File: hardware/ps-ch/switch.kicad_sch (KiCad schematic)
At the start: 0 parts

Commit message: did some wiring
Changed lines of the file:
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@@
 	(generator_version "9.0")
 	(paper "A4")
-	(hierarchical_label "OFF"
+	(hierarchical_label "ON{slash}~{OFF}"
 		(shape input)
-		(at 74.93 114.3 180)
+		(at 111.76 62.23 0)
 		(effects
 			(font
 				(size 1.27 1.27)
 			)
-			(justify right)
+			(justify left)
 		)
 	)
@@
 		(shape output)
 		(at 171.45 80.01 0)
+		(effects
+			(font
+				(size 1.27 1.27)
+			)
+			(justify left)
+		)
+	)
+	(hierarchical_label "ARM_OUTPUT"
+		(shape input)
+		(at 186.69 113.03 0)
 		(effects
 			(font
@@
 		)
 	)
-	(hierarchical_label "ON"
+	(hierarchical_label "~{OVC}"
 		(shape input)
-		(at 80.01 104.14 180)
+		(at 118.11 118.11 0)
 		(effects
 			(font
 				(size 1.27 1.27)
 			)
-			(justify right)
+			(justify left)
 		)
 	)

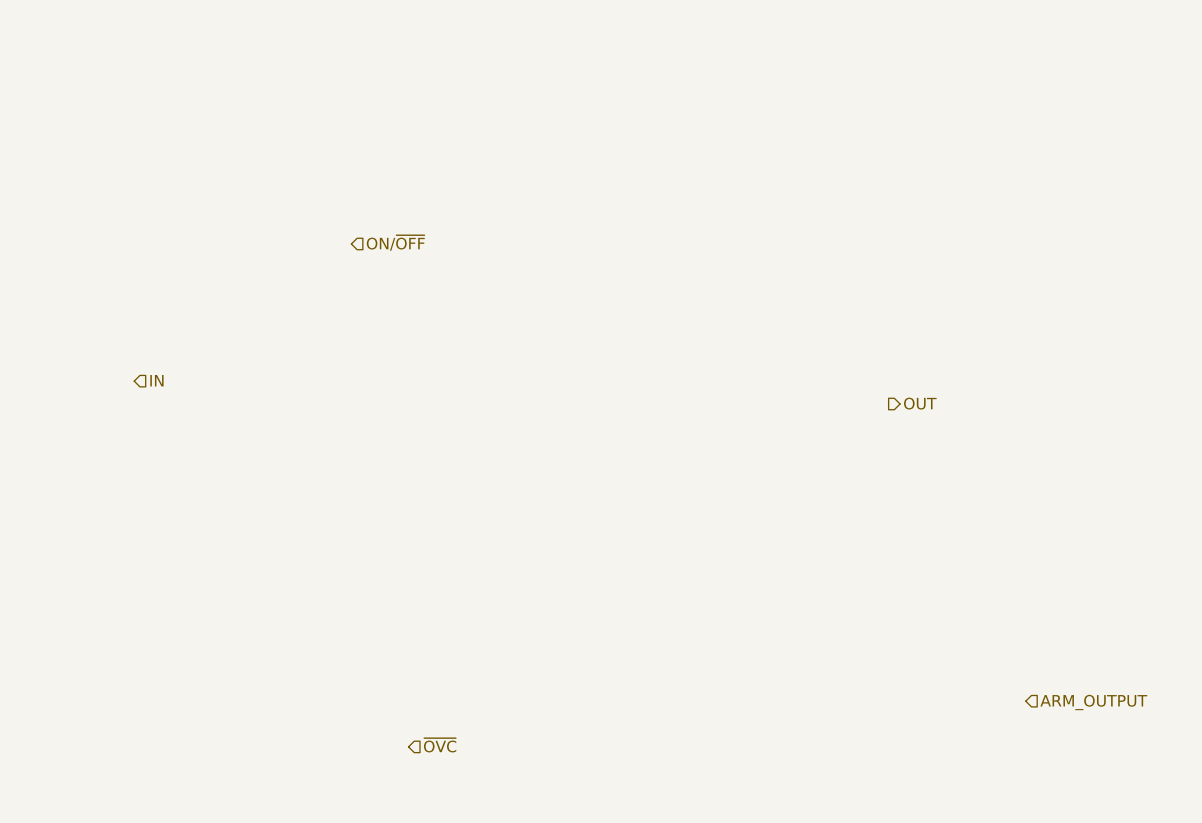
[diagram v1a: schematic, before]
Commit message: more wiring
- updated stm32 pinout
- added load switch
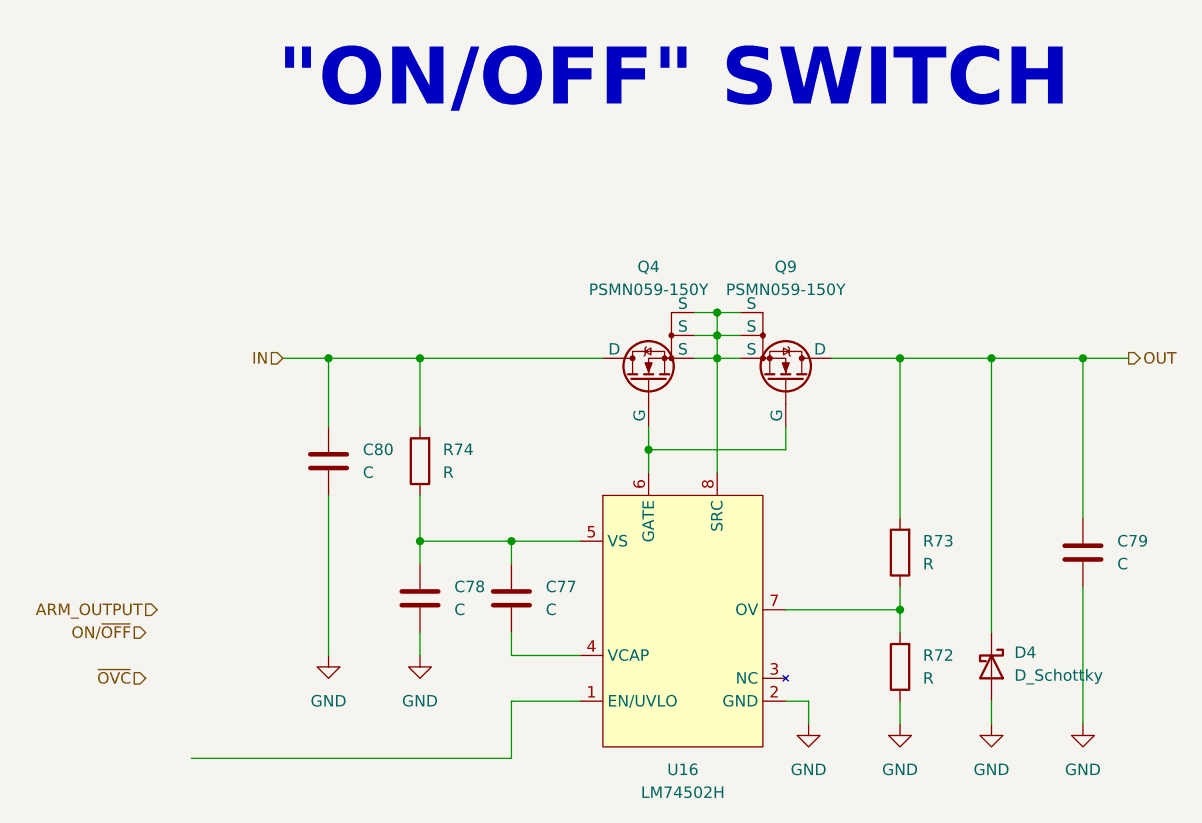
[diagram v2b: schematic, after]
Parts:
- added C77, C78, C79, C80: C, symbol Device:C
- added D4: D_Schottky, symbol Device:D_Schottky
- added Q4, Q9: PSMN059-150Y, symbol ps-ch:PSMN059-150Y
- added R72, R73, R74: R, symbol Device:R
- added U16: LM74502H, symbol ps-ch:LM74502H
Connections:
- net IN: now also C80.1, Q4.5 (D), R74.2
- net OUT: now also C79.1, D4.1 (K), Q9.5 (D), R73.2
- new net: C77.2, U16.4 (VCAP)
- new net: C77.1, C78.1, R74.1, U16.5 (VS)
- new net: Q4.4 (G), Q9.4 (G), U16.6 (GATE)
- new net: R72.2, R73.1, U16.7 (OV)
- new net: Q4.1 (S), Q4.2 (S), Q4.3 (S), Q9.1 (S), Q9.2 (S), Q9.3 (S), U16.8 (SRC)
- new net GND: C78.2, C79.2, C80.2, D4.2 (A), R72.1, U16.2 (GND)
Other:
- note added: ""ON/OFF" SWITCH"

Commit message: drawn enabled circuit
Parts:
- added D5: D_Schottky, symbol Device:D_Schottky
- added R28, R76, R77: R, symbol Device:R
- added U17, U18: 74LVC1G126, symbol 74xGxx:74LVC1G126
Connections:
- net ARM_OUTPUT: now also U18.1
- net GND: now also D5.2 (A), U17.3 (GND), U18.3 (GND)
- net IN: now also D5.1 (K)
- net ON/~{OFF}: now also R76.2, R77.2, U17.1
- net at U16.1 (EN/UVLO): now also U18.4
- new net: R76.1, U17.4, U18.2
- new net +3V3: U17.5 (VCC), U18.5 (VCC)
- new net MODE: R28.1, R77.1
- new net ~{OCP}: R28.2, U17.2
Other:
- moved on the sheet: C77, C78, C79, C80, D4, Q4, Q9, R72, R73, R74, U16

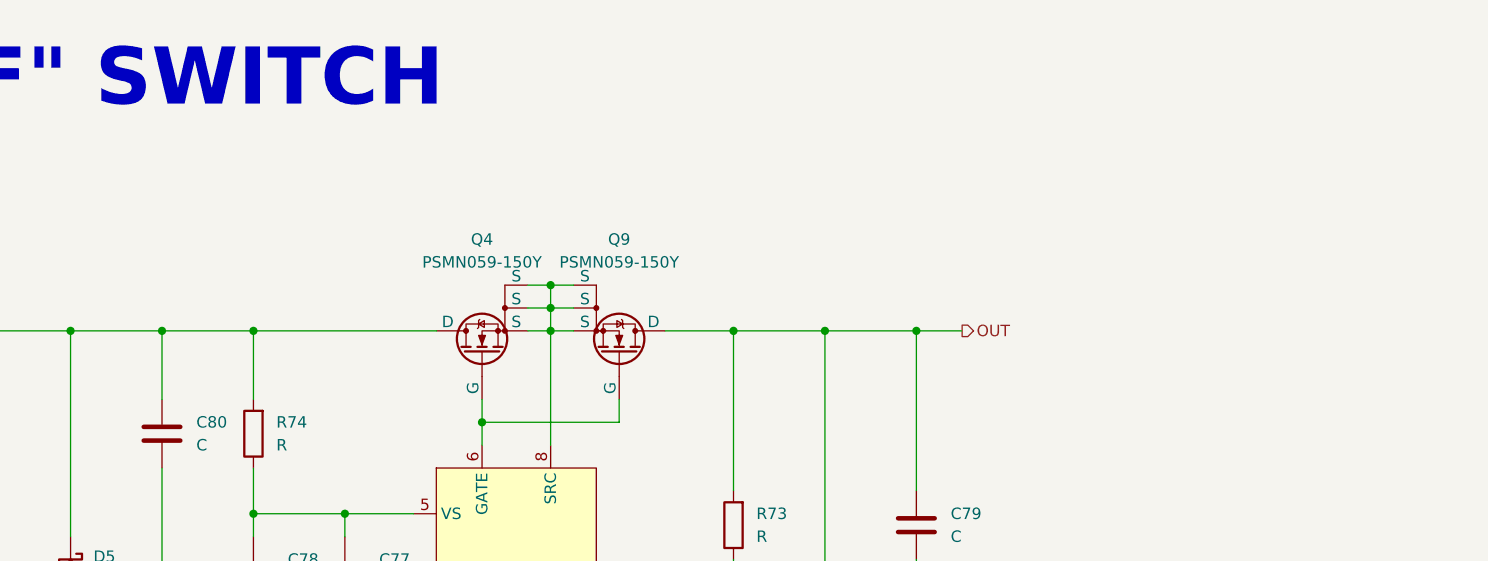
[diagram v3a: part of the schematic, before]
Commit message: Update switch.kicad_sch
- connected nmos driver to vdc
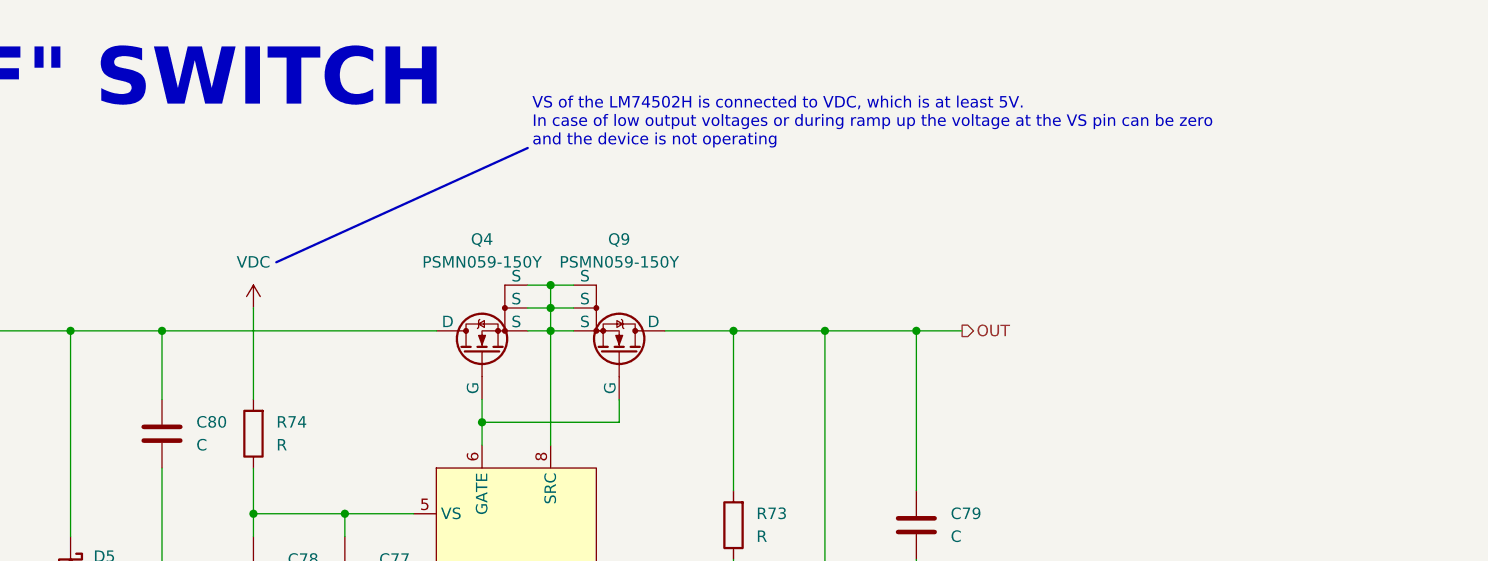
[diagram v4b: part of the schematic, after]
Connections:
- net IN: no longer R74.2
- new net VDC: R74.2
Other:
- note added: "VS of the LM74502H is connected to VDC, which is at least 5V. In case of low output voltages or during ramp up the voltage at the VS pin can be zero and the device is not operating"
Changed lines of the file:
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@@
 	(generator_version "9.0")
 	(paper "A4")
+	(text "VS of the LM74502H is connected to VDC, which is at least 5V.\nIn case of low output voltages or during ramp up the voltage at the VS pin can be zero\nand the device is not operating\n"
+		(exclude_from_sim no)
+		(at 191.008 48.006 0)
+		(effects
+			(font
+				(size 1.27 1.27)
+			)
+			(justify left)
+		)
+	)
 	(text "\"ON/OFF\" SWITCH"
 		(exclude_from_sim no)
@@
 	)
 	(junction
-		(at 160.02 71.12)
-		(diameter 0)
-		(color 0 0 0 0)
-	)
-	(junction
 		(at 149.86 71.12)
 		(diameter 0)
@@
 	(wire
 		(pts
-			(xy 149.86 71.12) (xy 160.02 71.12)
-		)
-		(stroke
-			(width 0)
-			(type default)
-		)
-	)
-	(wire
-		(pts
 			(xy 93.98 114.3) (xy 96.52 114.3)
 		)
@@
 	(wire
 		(pts
-			(xy 160.02 71.12) (xy 160.02 78.74)
-		)
-		(stroke
-			(width 0)
-			(type default)
-		)
-	)
-	(wire
-		(pts
 			(xy 68.58 119.38) (xy 76.2 119.38)
 		)
@@
 		)
 	)
+	(polyline
+		(pts
+			(xy 162.56 63.5) (xy 190.5 50.8)
+		)
+		(stroke
+			(width 0.254)
+			(type solid)
+		)
+	)
 	(wire
 		(pts
@@
 	(wire
 		(pts
+			(xy 160.02 68.58) (xy 160.02 78.74)
+		)
+		(stroke
+			(width 0)
+			(type default)
+		)
+	)
+	(wire
+		(pts
 			(xy 160.02 86.36) (xy 160.02 91.44)
 		)
@@
 	(wire
 		(pts
-			(xy 160.02 71.12) (xy 180.34 71.12)
+			(xy 149.86 71.12) (xy 180.34 71.12)
 		)
 		(stroke
@@
 					(unit 1)
 				)
+			)
+		)
+	)
+	(symbol
+		(lib_id "power:VDC")
+		(at 160.02 68.58 0)
+		(unit 1)
+		(exclude_from_sim no)
+		(in_bom yes)
+		(on_board yes)
+		(dnp no)
+		(fields_autoplaced yes)
+		(property "Reference" "#PWR0138"
+			(at 160.02 72.39 0)
+			(effects
+				(font
+					(size 1.27 1.27)
+				)
+				(hide yes)
+			)
+		)
+		(property "Value" "VDC"
+			(at 160.02 63.5 0)
+			(effects
+				(font
+					(size 1.27 1.27)
+				)
+			)
+		)
+		(property "Footprint" ""
+			(at 160.02 68.58 0)
+			(effects
+				(font
+					(size 1.27 1.27)
+				)
+				(hide yes)
+			)
+		)
+		(property "Datasheet" ""
+			(at 160.02 68.58 0)
+			(effects
+				(font
+					(size 1.27 1.27)
+				)
+				(hide yes)
+			)
+		)
+		(property "Description" "Power symbol creates a global label with name \"VDC\""
+			(at 160.02 68.58 0)
+			(effects
+				(font
+					(size 1.27 1.27)
+				)
+				(hide yes)
+			)
+		)
+		(pin "1"
+		)
+		(instances
+			(project "ps-ch"
+				(path "/431acd2e-2ab9-4aa9-b759-273f044decc5/8b075681-8e5e-4240-bfaa-b14997f80de9"
+					(reference "#PWR0138")
+					(unit 1)
+				)

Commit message: Update switch.kicad_sch
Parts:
- added R78: R, symbol Device:R
- added U19: 74LVC1G126, symbol 74xGxx:74LVC1G126
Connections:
- net +3V3: now also R28.1, R78.1, U19.5 (VCC)
- net GND: now also R77.2, U19.3 (GND)
- net MODE: now also U17.1; no longer R28.1, R77.1
- net ON/~{OFF}: now also U19.1; no longer R77.2, U17.1
- net at R76.1, U18.2: now also U19.4; no longer U17.4
- net at U16.1 (EN/UVLO), U18.4: now also R77.1
- new net: R78.2, U17.4, U19.2
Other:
- note added: "replace by quad buffer (74LVC126A)"
- moved on the sheet: C77, C78, C79, C80, D4, D5, Q4, Q9, R28, R72, R73, R74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

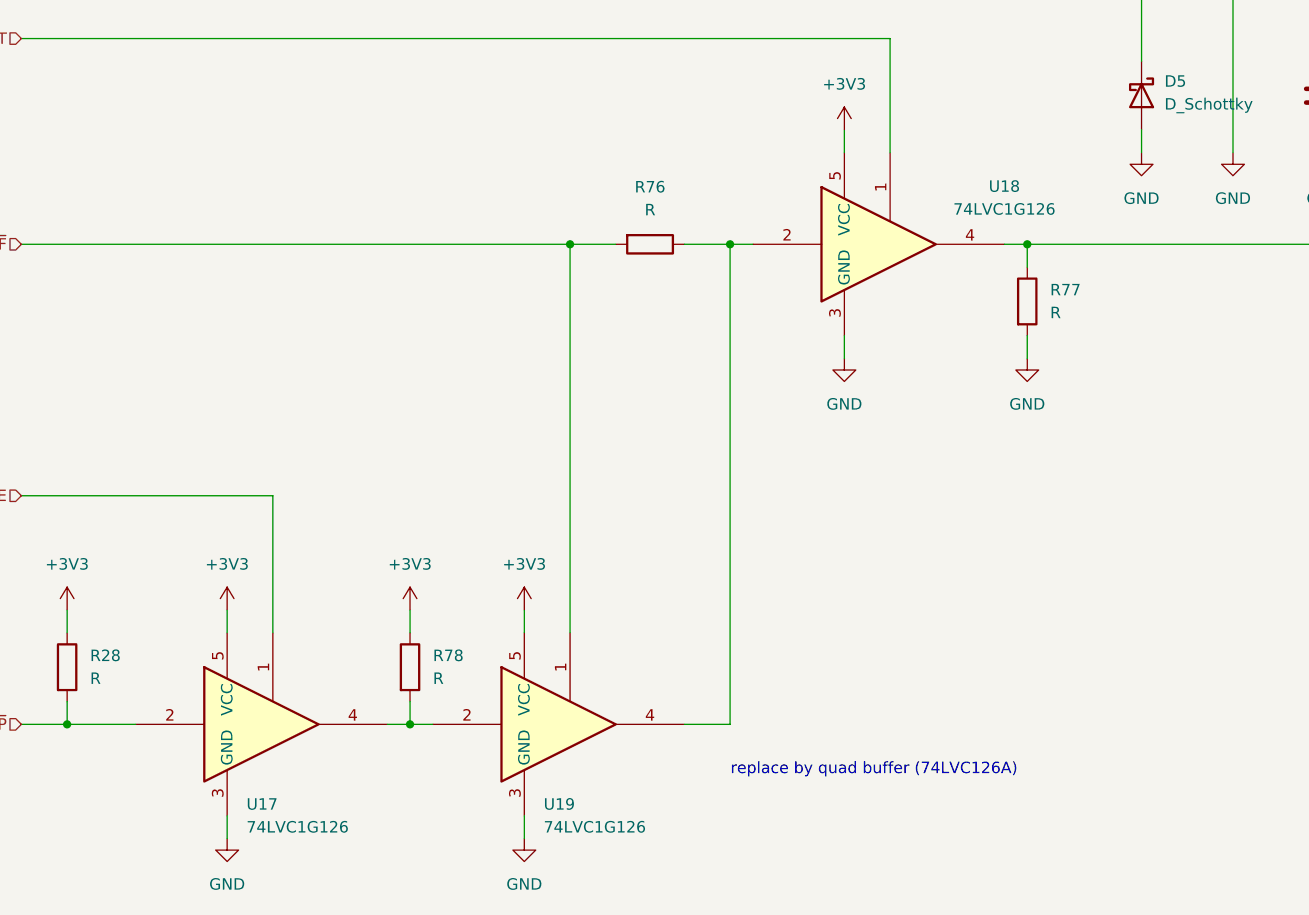
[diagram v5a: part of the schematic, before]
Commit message: added 74LVC126A
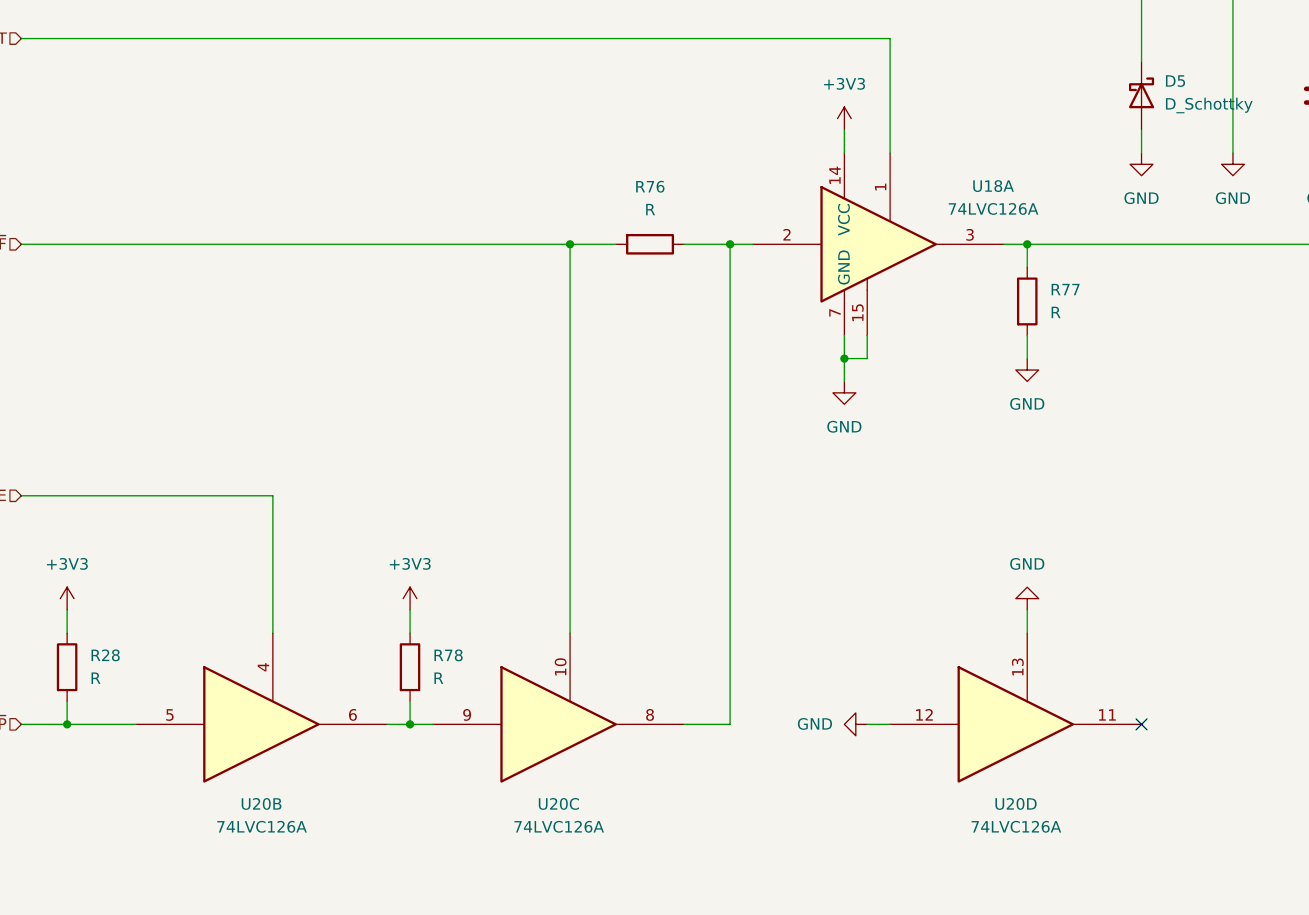
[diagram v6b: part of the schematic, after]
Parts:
- removed U17, U18, U19: 74LVC1G126, symbol 74xGxx:74LVC1G126
- added U18, U20: 74LVC126A, symbol ps-ch:74LVC126A
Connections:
- net +3V3: now also U18.14 (VCC)
- net ARM_OUTPUT: now also U18.1
- net GND: now also U18.15, U18.7 (GND), U20.12, U20.13
- net MODE: now also U20.4
- net ON/~{OFF}: now also U20.10
- net ~{OCP}: now also U20.5
- net at R76.1: now also U18.2, U20.8
- net at R77.1, U16.1 (EN/UVLO): now also U18.3
- net at R78.2: now also U20.6, U20.9
- no-connect marks 0 -> 1
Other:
- note removed: "replace by quad buffer (74LVC126A)"
